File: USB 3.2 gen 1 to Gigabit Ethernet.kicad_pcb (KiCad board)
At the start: 4 copper layers, 50 x 27.5 mm, 53 parts, among them J1 USB_C_Receptacle, U1 VL162, U2 RTL8153-VC-CG, U3 W25Q16BVSSIG, U4 TLV70233DBVR, Y1 25Mhz

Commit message: Uploaded pics
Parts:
- added G***: LOGO, LOGO, B.Cu at (193.8, 103.8)
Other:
- board text added: "Designed by Cath 2025"
- board text added: "USB Type C to Gigabit Ethernet"
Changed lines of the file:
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@@
 		)
 	)
+	(footprint "LOGO"
+		(layer "B.Cu")
+		(at 193.85 103.85 180)
+		(property "Reference" "G***"
+			(at 0 0 0)
+			(layer "B.SilkS")
+			(hide yes)
+			(effects
+				(font
+					(size 1.5 1.5)
+					(thickness 0.3)
+				)
+				(justify mirror)
+			)
+		)
+		(property "Value" "LOGO"
+			(at 0.75 0 0)
+			(layer "B.SilkS")
+			(hide yes)
+			(effects
+				(font
+					(size 1.5 1.5)
+					(thickness 0.3)
+				)
+				(justify mirror)
+			)
+		)
+		(property "Footprint" ""
+			(at 0 0 0)
+			(unlocked yes)
+			(layer "B.Fab")
+			(hide yes)
+			(effects
+				(font
+					(size 1.27 1.27)
+					(thickness 0.15)
+				)
+				(justify mirror)
+			)
+		)
+		(property "Datasheet" ""
+			(at 0 0 0)
+			(unlocked yes)
+			(layer "B.Fab")
+			(hide yes)
+			(effects
+				(font
+					(size 1.27 1.27)
+					(thickness 0.15)
+				)
+				(justify mirror)
+			)
+		)
+		(property "Description" ""
+			(at 0 0 0)
+			(unlocked yes)
+			(layer "B.Fab")
+			(hide yes)
+			(effects
+				(font
+					(size 1.27 1.27)
+					(thickness 0.15)
+				)
+				(justify mirror)
+			)
+		)
+		(attr board_only exclude_from_pos_files exclude_from_bom)
+		(fp_poly
+			(pts
+				(xy -1.180023 2.442259) (xy -1.067589 2.428412) (xy -0.956964 2.405468) (xy -0.848412 2.373503)
+				(xy -0.7422 2.332591) (xy -0.63859 2.282807) (xy -0.537849 2.224227) (xy -0.465711 2.17555) (xy -0.373102 2.103576)
+				(xy -0.284662 2.023328) (xy -0.200607 1.935032) (xy -0.121153 1.838918) (xy -0.046515 1.735213)
+				(xy -0.04296 1.729901) (xy -0.029069 1.709342) (xy -0.016851 1.691749) (xy -0.007302 1.678523) (xy -0.001421 1.671062)
+				(xy -0.000192 1.669938) (xy 0.003742 1.673028) (xy 0.011162 1.682445) (xy 0.020759 1.69646) (xy 0.02547 1.703856)
+				(xy 0.07244 1.774213) (xy 0.126166 1.845916) (xy 0.184752 1.916693) (xy 0.246302 1.984276) (xy 0.308922 2.046393)
+				(xy 0.320218 2.056872) (xy 0.411113 2.134304) (xy 0.505841 2.203454) (xy 0.604097 2.264206) (xy 0.705575 2.316443)
+				(xy 0.809969 2.360048) (xy 0.916974 2.394905) (xy 1.026284 2.420896) (xy 1.137593 2.437906) (xy 1.250596 2.445817)
+				(xy 1.338446 2.445639) (xy 1.450697 2.438185) (xy 1.558043 2.423261) (xy 1.661586 2.400595) (xy 1.762425 2.369918)
+				(xy 1.861662 2.330958) (xy 1.924991 2.301479) (xy 2.023814 2.24757) (xy 2.116796 2.186407) (xy 2.203687 2.118263)
+				(xy 2.284237 2.043409) (xy 2.358198 1.962118) (xy 2.42532 1.874661) (xy 2.485354 1.78131) (xy 2.538051 1.682339)
+				(xy 2.579695 1.586914) (xy 2.607319 1.51066) (xy 2.630061 1.43412) (xy 2.648698 1.354362) (xy 2.663696 1.270469)
+				(xy 2.666509 1.251642) (xy 2.66878 1.234181) (xy 2.670567 1.21678) (xy 2.671926 1.198137) (xy 2.672916 1.176944)
+				(xy 2.673593 1.151898) (xy 2.674016 1.121693) (xy 2.674242 1.085025) (xy 2.674328 1.040589) (xy 2.674334 1.029033)
+				(xy 2.674174 0.969985) (xy 2.673581 0.918465) (xy 2.672453 0.872633) (xy 2.670689 0.830646) (xy 2.668186 0.790664)
+				(xy 2.664844 0.750845) (xy 2.66056 0.709348) (xy 2.655232 0.664331) (xy 2.653343 0.649299) (xy 2.63296 0.516875)
+				(xy 2.606009 0.389938) (xy 2.572171 0.267783) (xy 2.531128 0.149704) (xy 2.482558 0.034995) (xy 2.426145 -0.07705)
+				(xy 2.361568 -0.187137) (xy 2.288509 -0.295972) (xy 2.206649 -0.40426) (xy 2.141578 -0.482872) (xy 2.111949 -0.51711)
+				(xy 2.082259 -0.550722) (xy 2.052132 -0.584059) (xy 2.021193 -0.617473) (xy 1.989065 -0.651316)
+				(xy 1.955374 -0.685941) (xy 1.919742 -0.721699) (xy 1.881796 -0.758943) (xy 1.841159 -0.798024)
+				(xy 1.797454 -0.839295) (xy 1.750308 -0.883108) (xy 1.699343 -0.929814) (xy 1.644184 -0.979766)
+				(xy 1.584456 -1.033316) (xy 1.519782 -1.090816) (xy 1.449787 -1.152618) (xy 1.374095 -1.219074)
+				(xy 1.292331 -1.290536) (xy 1.204119 -1.367356) (xy 1.115952 -1.443927) (xy 1.007926 -1.537785)
+				(xy 0.906611 -1.626115) (xy 0.811499 -1.70937) (xy 0.722084 -1.788005) (xy 0.637857 -1.862477) (xy 0.558312 -1.933238)
+				(xy 0.482941 -2.000745) (xy 0.411235 -2.065451) (xy 0.342689 -2.127812) (xy 0.276794 -2.188283)
+				(xy 0.213043 -2.247317) (xy 0.150929 -2.305371) (xy 0.089944 -2.362899) (xy 0.079096 -2.373186)
+				(xy 0.056793 -2.394278) (xy 0.036827 -2.413012) (xy 0.020174 -2.428485) (xy 0.00781 -2.439793) (xy 0.00071 -2.446034)
+				(xy -0.000601 -2.446978) (xy -0.004408 -2.443831) (xy -0.013708 -2.435304) (xy -0.027269 -2.422552)
+				(xy -0.043856 -2.406727) (xy -0.051569 -2.399306) (xy -0.06726 -2.384317) (xy -0.088568 -2.364172)
+				(xy -0.114216 -2.340069) (xy -0.142926 -2.313204) (xy -0.173419 -2.284776) (xy -0.204417 -2.25598)
+				(xy -0.22034 -2.241233) (xy -0.269188 -2.196096) (xy -0.315886 -2.15307) (xy -0.360967 -2.111683)
+				(xy -0.404961 -2.071462) (xy -0.4484 -2.031937) (xy -0.491815 -1.992636) (xy -0.535739 -1.953086)
+				(xy -0.580702 -1.912815) (xy -0.627235 -1.871352) (xy -0.675871 -1.828225) (xy -0.727141 -1.782961)
+				(xy -0.781576 -1.73509) (xy -0.839707 -1.684139) (xy -0.902067 -1.629636) (xy -0.969186 -1.571109)
+				(xy -1.041595 -1.508087) (xy -1.119828 -1.440097) (xy -1.204414 -1.366668) (xy -1.242348 -1.333757)
+				(xy -1.334607 -1.253545) (xy -1.420036 -1.178867) (xy -1.49906 -1.109317) (xy -1.572106 -1.044492)
+				(xy -1.6396 -0.983988) (xy -1.701968 -0.9274) (xy -1.759637 -0.874324) (xy -1.813032 -0.824357)
+				(xy -1.862579 -0.777094) (xy -1.908706 -0.73213) (xy -1.951837 -0.689062) (xy -1.9924 -0.647486)
+				(xy -2.03082 -0.606997) (xy -2.067523 -0.567191) (xy -2.102936 -0.527664) (xy -2.137485 -0.488012)
+				(xy -2.151901 -0.471151) (xy -2.239907 -0.362216) (xy -2.318843 -0.252863) (xy -2.389011 -0.142479)
+				(xy -2.450715 -0.030453) (xy -2.504258 0.083825) (xy -2.549944 0.200968) (xy -2.588076 0.321586)
+				(xy -2.618958 0.446291) (xy -2.627303 0.486879) (xy -2.640375 0.558229) (xy -2.651057 0.627281)
+				(xy -2.65951 0.695892) (xy -2.665898 0.765918) (xy -2.670382 0.839214) (xy -2.673126 0.917636) (xy -2.674292 1.00304)
+				(xy -2.674355 1.024345) (xy -2.674365 1.070556) (xy -2.674243 1.108719) (xy -2.673931 1.140161)
+				(xy -2.67337 1.166211) (xy -2.672502 1.188195) (xy -2.671269 1.207443) (xy -2.669612 1.22528) (xy -2.667473 1.243036)
+				(xy -2.664793 1.262038) (xy -2.663528 1.270469) (xy -2.642197 1.383761) (xy -2.613294 1.491872)
+				(xy -2.576641 1.595387) (xy -2.539029 1.680676) (xy -2.485939 1.78011) (xy -2.425741 1.87363) (xy -2.35879 1.960996)
+				(xy -2.285443 2.041968) (xy -2.206057 2.116305) (xy -2.120988 2.183768) (xy -2.030591 2.244116)
+				(xy -1.935224 2.297109) (xy -1.835242 2.342506) (xy -1.731002 2.380068) (xy -1.62286 2.409555) (xy -1.511172 2.430726)
+				(xy -1.409259 2.442364) (xy -1.294001 2.446935)
+			)
+			(stroke
+				(width 0)
+				(type solid)
+			)
+			(fill solid)
+			(layer "B.SilkS")
+		)
+	)
 	(footprint "Capacitor_SMD:C_0402_1005Metric"
 		(layer "B.Cu")
@@
 		(layer "Edge.Cuts")
 	)
+	(gr_text "USB Type C \nto Gigabit Ethernet"
+		(at 193.9 124.05 0)
+		(layer "B.SilkS")
+		(effects
+			(font
+				(size 1 1)
+				(thickness 0.2)
+				(bold yes)
+			)
+			(justify left bottom mirror)
+		)
+	)
+	(gr_text "Designed \n by Cath\n  2025\n\n\n"
+		(at 203.6 109.05 0)
+		(layer "B.SilkS")
+		(effects
+			(font
+				(size 1 1)
+				(thickness 0.2)
+				(bold yes)
+			)
+			(justify left bottom mirror)
+		)
+	)
 	(segment

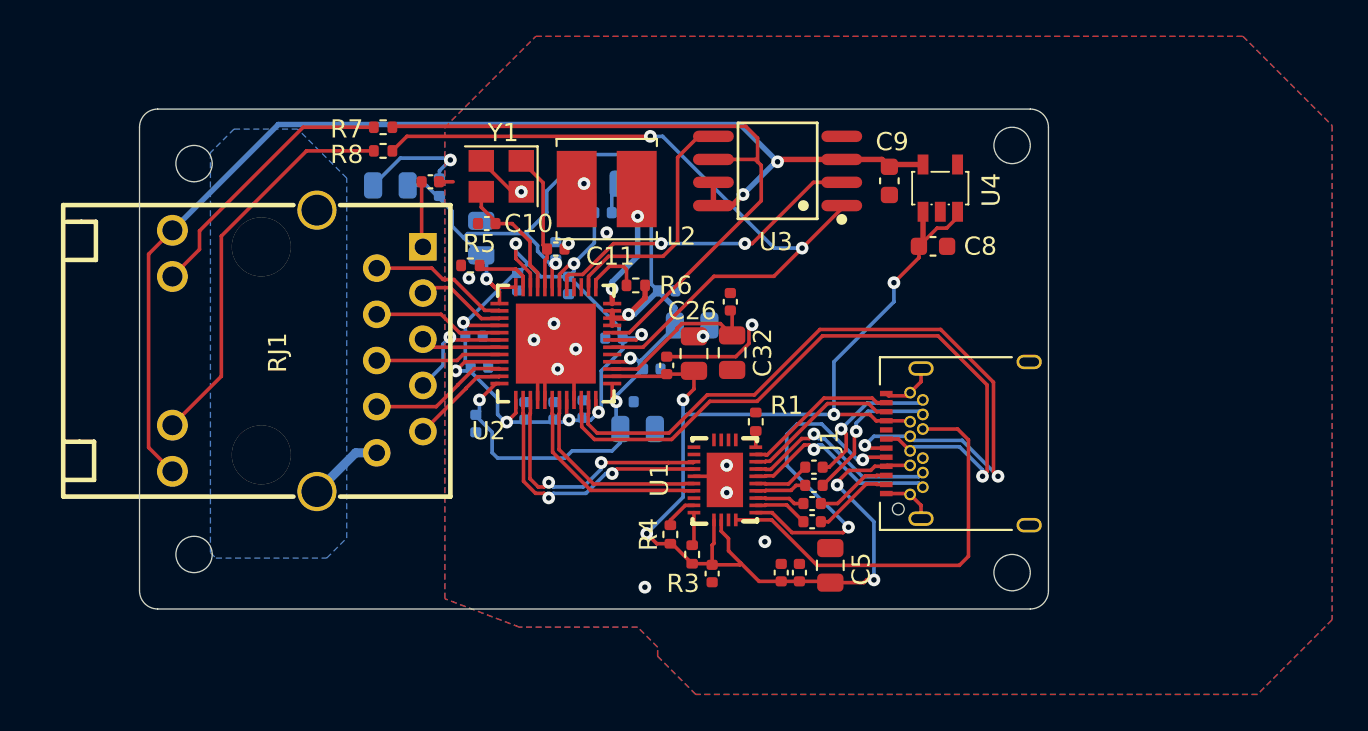
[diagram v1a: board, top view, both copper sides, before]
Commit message: Fixed usb footprint
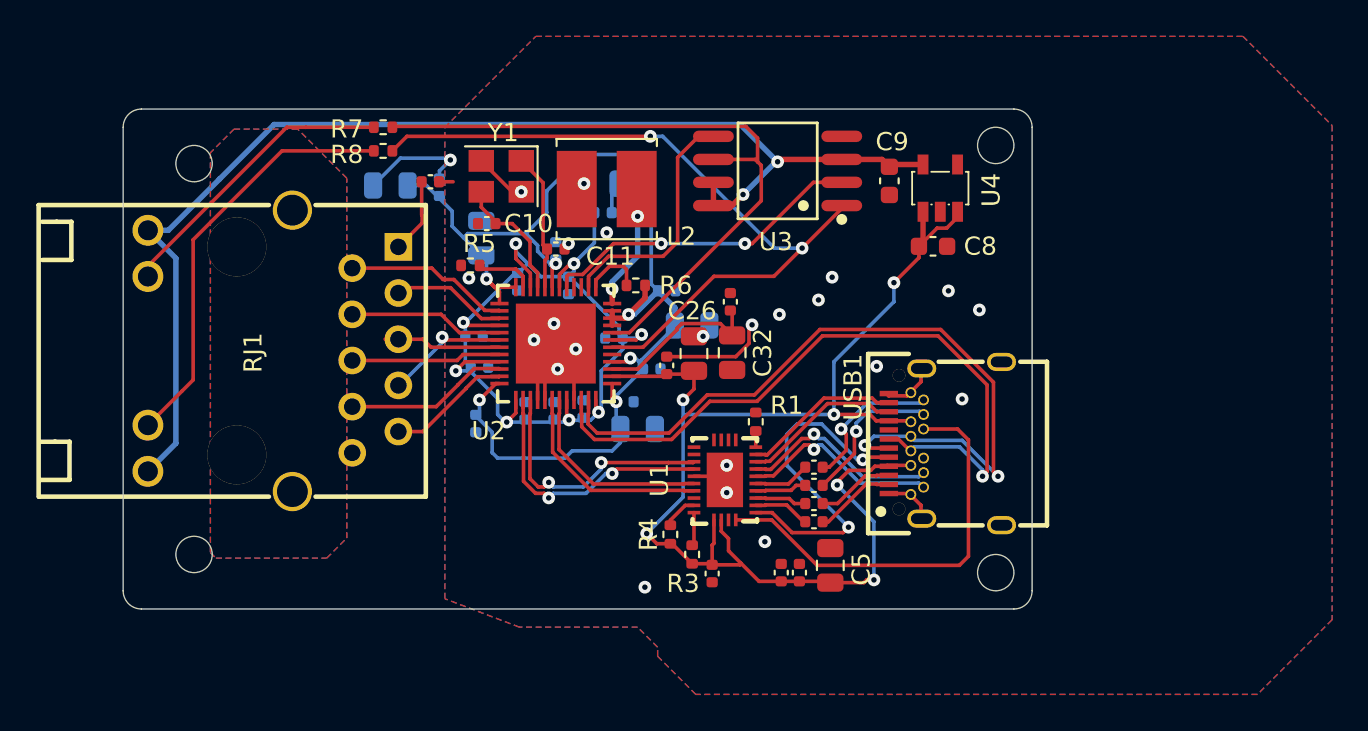
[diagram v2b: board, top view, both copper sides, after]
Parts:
- removed J1: USB_C_Receptacle, Connector_USB:USB_C_Receptacle_Amphenol_12401548E4-2A
- added USB1: TYPEC-324-BCP24, da:USB-C-SMD_TYPEC-324-BCP24, F.Cu at (200.3, 116.5)
- moved RJ1 1.35 mm to (163.3, 111.4)
- moved C1 0.10 mm to (193.1, 119.8)
- moved C2 0.10 mm to (193.1, 120.8)
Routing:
- net ETH_Shield: track 4.17 -> 0.00 mm
- net MDIP2: track 4.39 -> 6.47 mm
- net +3.3V_2: track 65.0 -> 66.5 mm
- net MDIP3: track 7.64 -> 8.99 mm
- net MDIP1: track 7.17 -> 8.52 mm
- net MDIP0: track 7.72 -> 9.07 mm
- net MDIN2: track 6.89 -> 8.24 mm
- net MDIN0: track 5.05 -> 6.40 mm
- net MDIN3: track 5.48 -> 6.83 mm
- net Net-(R8-Pad1): track 21.8 -> 23.2 mm
- net Net-(R7-Pad2): track 15.1 -> 16.2 mm
- net MDIN1: track 6.05 -> 6.90 mm
- net Net-(C37-Pad1): track 3.61 -> 4.14 mm
- net GND: vias 15 -> 22
- added copper zone on F.Cu, net ETH_Shield
- added copper zone on In1.Cu, net ETH_Shield
- added copper zone on In2.Cu, net ETH_Shield
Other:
- outline, holes or cut-outs redrawn
